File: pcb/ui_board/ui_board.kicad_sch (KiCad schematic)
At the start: 134 parts, among them J1 PWR3.3V, J2 UI, J3 Conn_02x03_Odd_Even, Q1 BSS138, Q2 IRLML6402, Q3 IRLML6402, Q4 IRLML6402, Q5 IRLML6402, Q6 IRLML6402, Q7 IRLML6402, Q8 IRLML6402, SW1 SW_CHAN, SW10 SW_8, SW11 SW_5, SW12 SW_2, SW13 SW_DP, SW14 SW_9, SW15 SW_6, SW16 SW_3, SW17 SW_DP, SW18 SW_LEFT, SW19 SW_RIGHT, SW2 SW_MODE, SW20 SW_ENTER, SW21 SW_BACK_DISP, SW22 SW_INPUT, SW23 SW_RUN_STOP, SW24 SW_SINGLE, SW25 PEC11H-4225F-S0024, SW3 SW_MENU, SW4 SW_SHIFT, SW5 OMRB3FS, SW6 SW_7, SW7 SW_4, SW8 SW_1, SW9 SW_0, U1 STM32L010C6, U10 STP16CP05, U2 DYSR00P401101, U3 STP16CP05, U4 STP16CP05, U5 DYSR00P401101, U6 STP16CP05, U7 74HC14, U8 STP16CP05, U9 DYSR00P401101, Y1 16MHz

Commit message: Add power supply board and minor improvements
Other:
- company: (none) -> Sebastian Harnisch
- title: (none) -> UI Board for Programmable Precision Resistor
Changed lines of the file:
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@@
 (kicad_sch (version 20230121) (generator eeschema)
   (paper "A3")
+  (title_block
+    (title "UI Board for Programmable Precision Resistor")
+    (date "2023-08-19")
+    (rev "B")
+    (company "Sebastian Harnisch")
+  )
   (junction (at 41.91 25.4) (diameter 0) (color 0 0 0 0)
   )

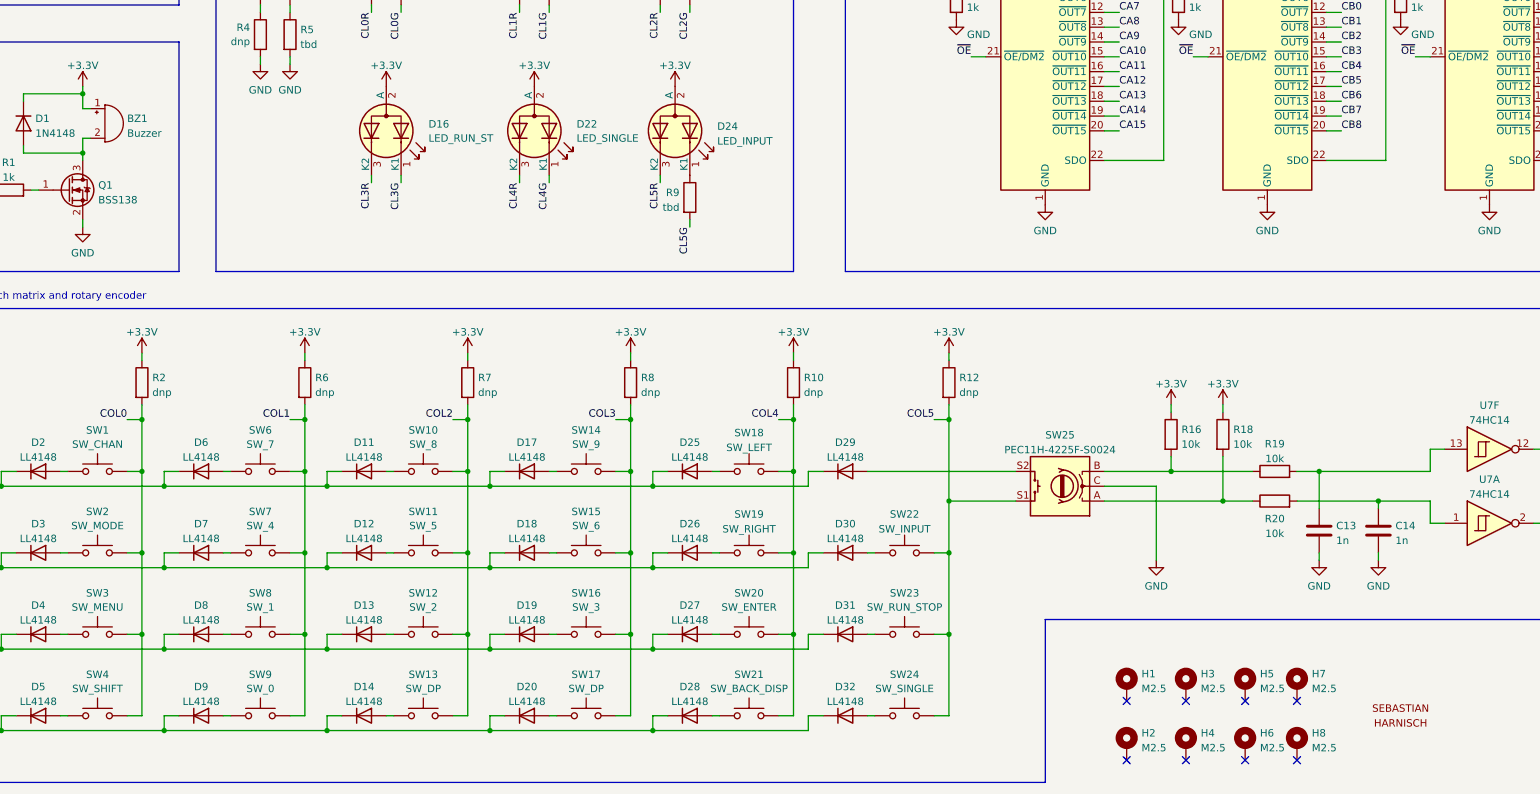
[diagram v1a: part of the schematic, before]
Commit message: Update to Kicad v9, new power supply board and other modifications
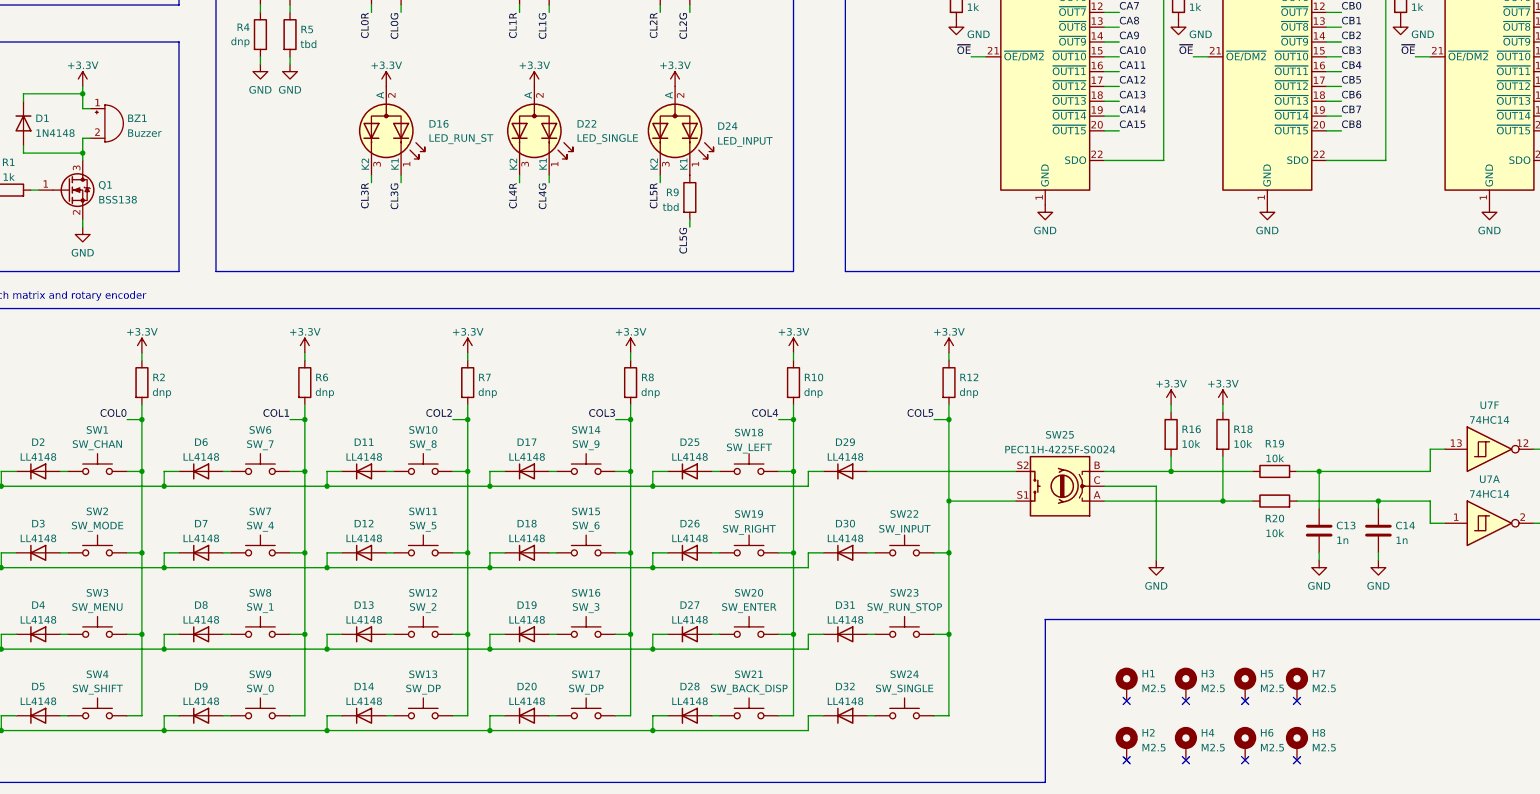
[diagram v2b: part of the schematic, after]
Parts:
- removed LOGO1: LOGO_SH, 01_Sebastian:SebastianHarnisch, symbol 01_Sebastian:LOGO_SH
